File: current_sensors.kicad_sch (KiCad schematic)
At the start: 56 parts, among them U2 LM2902, U3 LM2902, U4 LM2902, U5 LM2902, U6 LM2902, U7 LM2902

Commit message: cleaning up
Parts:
- R10, R11, R12, R13, R14, R23, R24, R25, R26, R35, R36, R37, R38, R62: value R -> 47k
- R19, R20, R21, R22, R31, R32, R33, R34, R5, R6, R7, R8, R9: value R -> 10k
- R4: value R -> 0R39

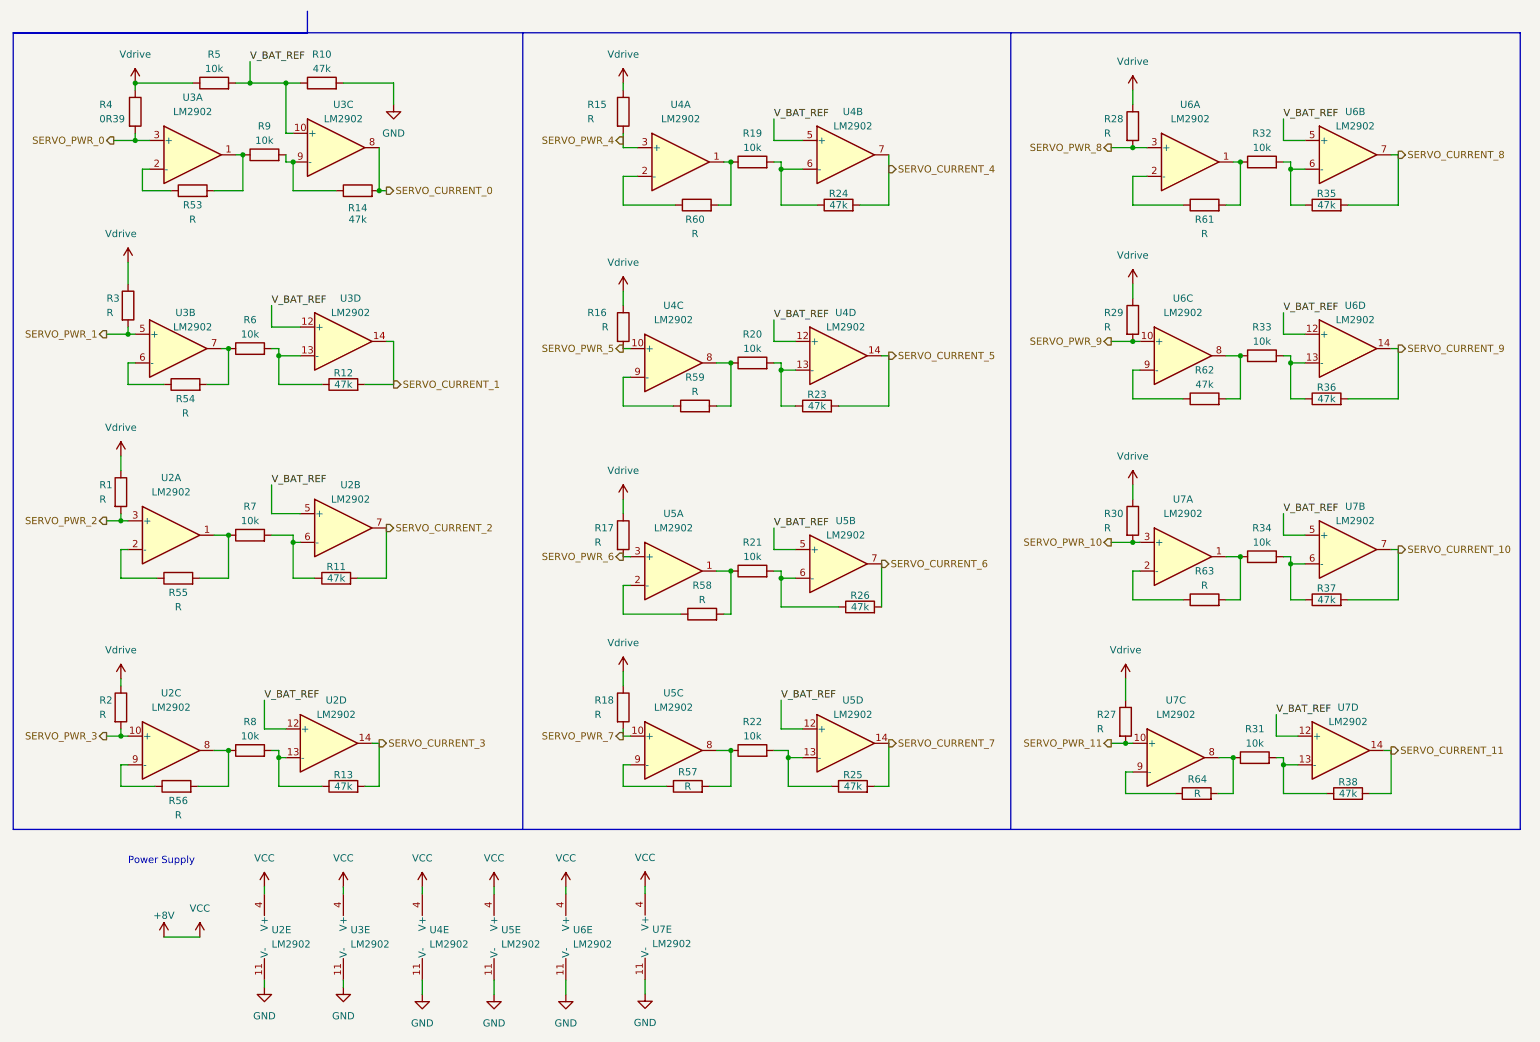
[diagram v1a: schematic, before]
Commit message: Bord v1.2, added flash memory, changed pinout od servomotor connectors and removed potentiometer signal from servomotors plus one ADC
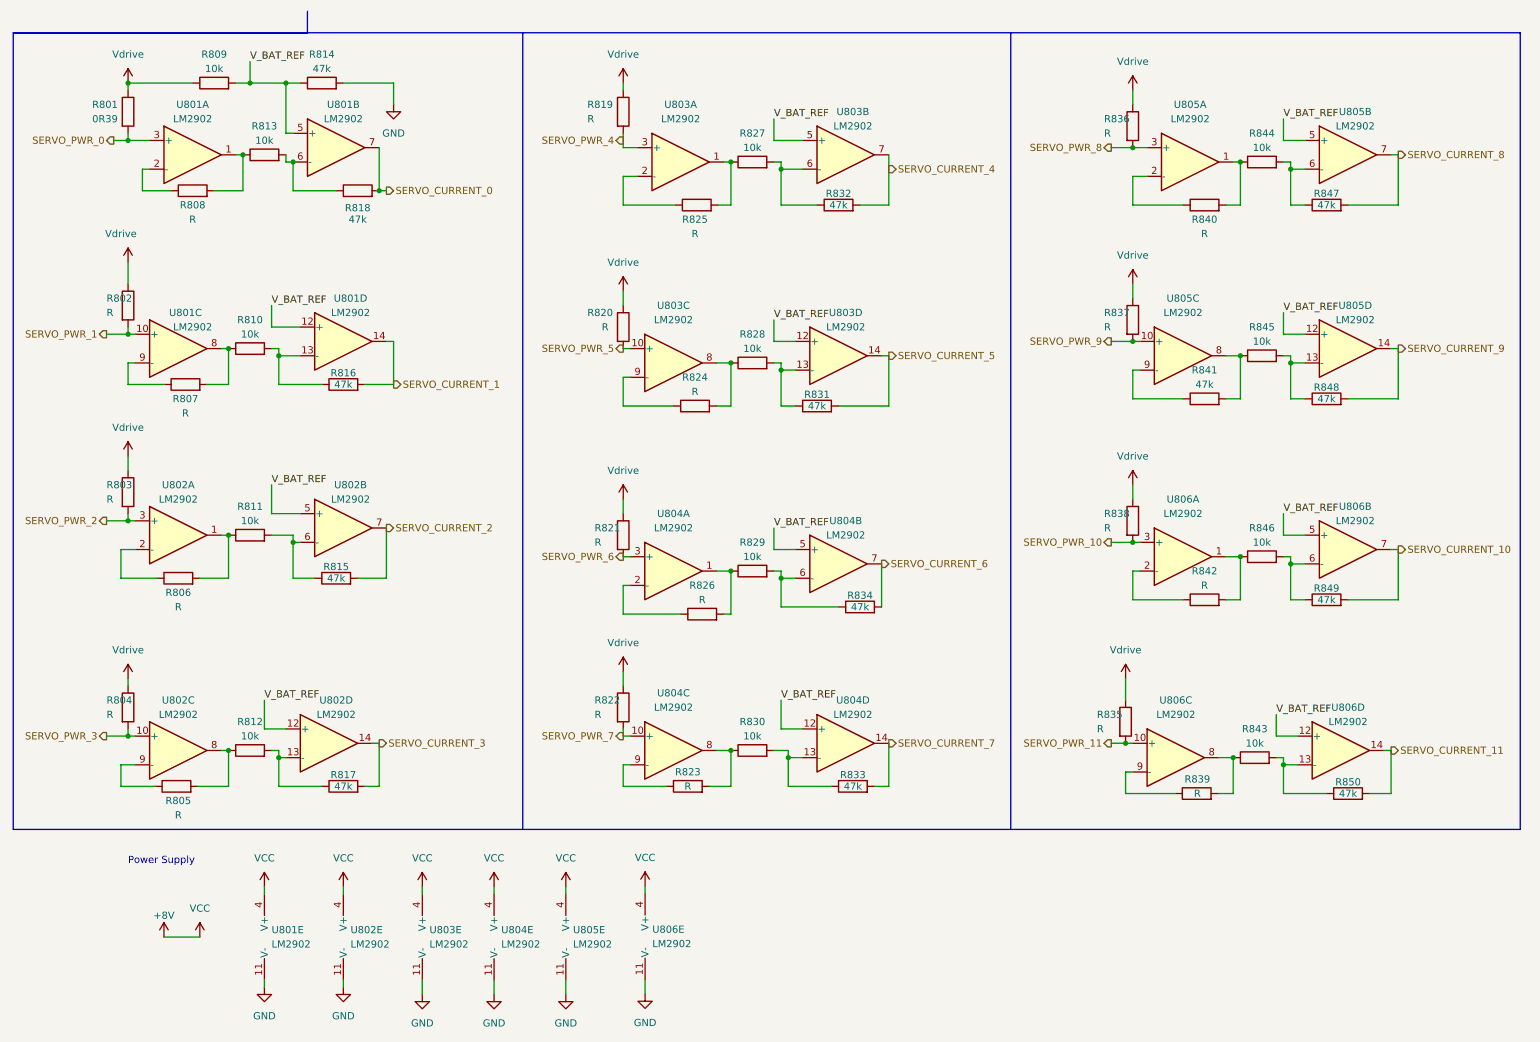
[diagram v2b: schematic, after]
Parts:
- renumbered R4 to R801, R3 to R802, R1 to R803, R2 to R804, R56 to R805, R55 to R806, R54 to R807, R53 to R808, R5 to R809, R6 to R810, R7 to R811, R8 to R812, R9 to R813, R10 to R814, R11 to R815, R12 to R816, R13 to R817, R14 to R818, R15 to R819, R16 to R820, R17 to R821, R18 to R822, R57 to R823, R59 to R824, R60 to R825, R58 to R826, R19 to R827, R20 to R828, R21 to R829, R22 to R830, R23 to R831, R24 to R832, R25 to R833, R26 to R834, R27 to R835, R28 to R836, R29 to R837, R30 to R838, R64 to R839, R61 to R840, R62 to R841, R63 to R842, R31 to R843, R32 to R844, R33 to R845, R34 to R846, R35 to R847, R36 to R848, R37 to R849, R38 to R850, U3 to U801, U2 to U801, U2 to U802, U3 to U802, U4 to U803, U5 to U804, U6 to U805, U7 to U806
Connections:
- net SERVO_CURRENT_0: now also U801.7; no longer U801.8
- net SERVO_PWR_1: now also U801.10 (+); no longer U801.5 (+)
- net V_BAT_REF: now also U801.5 (+); no longer U801.10 (+)
- net at R807.2, R810.1: now also U801.8; no longer U801.7
- net at R807.1: now also U801.9 (-); no longer U801.6 (-)
- net at R813.2, R818.1: now also U801.6 (-); no longer U801.9 (-)
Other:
- moved on the sheet: R801, R803, R804, U802A, U802C
